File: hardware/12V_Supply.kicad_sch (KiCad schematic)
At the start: 27 parts, among them J1 353180620, J4002 353180620, J4003 353180620, U17 ACS758xCB-150B-PSS

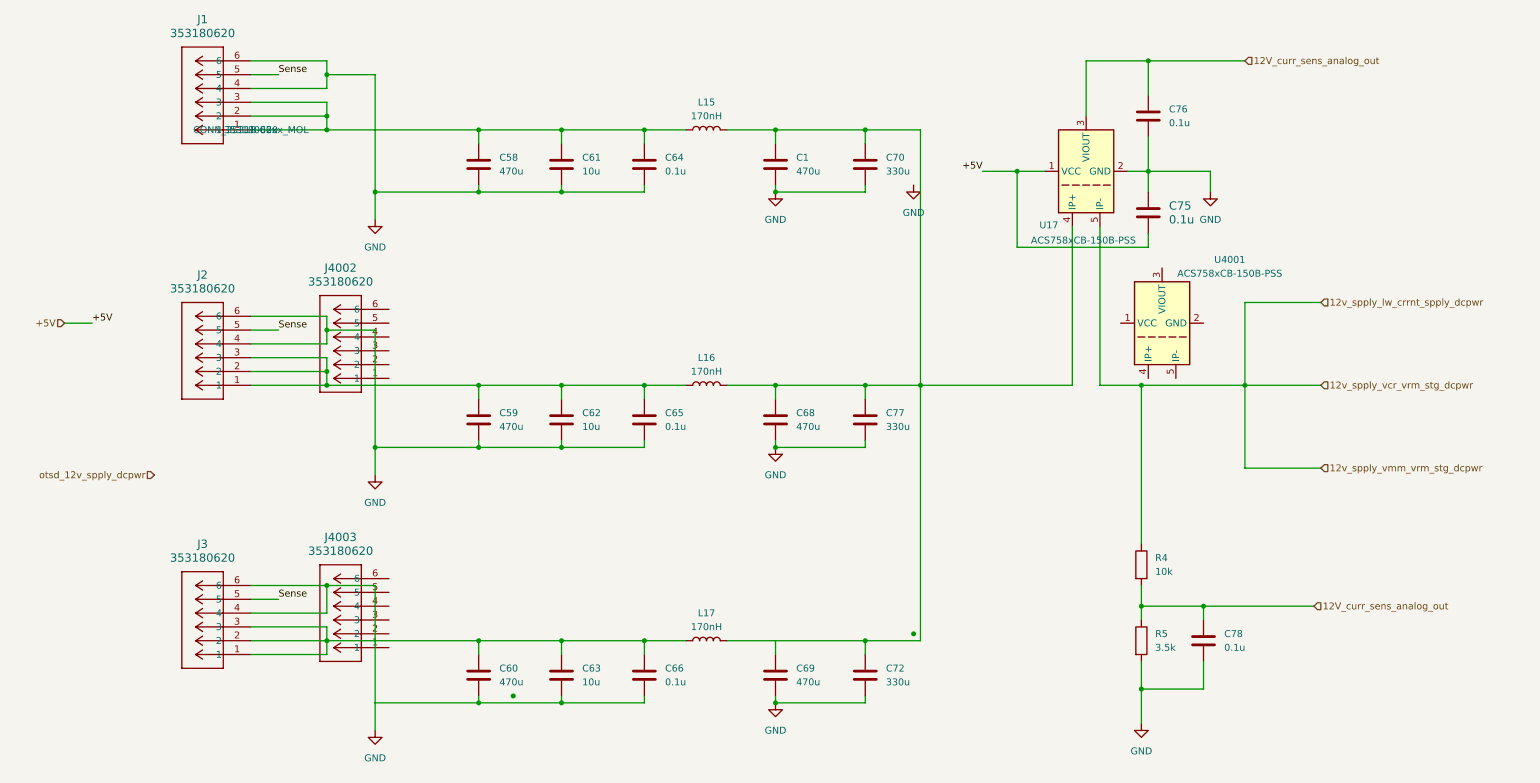
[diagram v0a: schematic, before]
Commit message: fix(schematic): 12V Supply & Low Current Supply
Added proper switching 5V and linear 3.3V ICs.
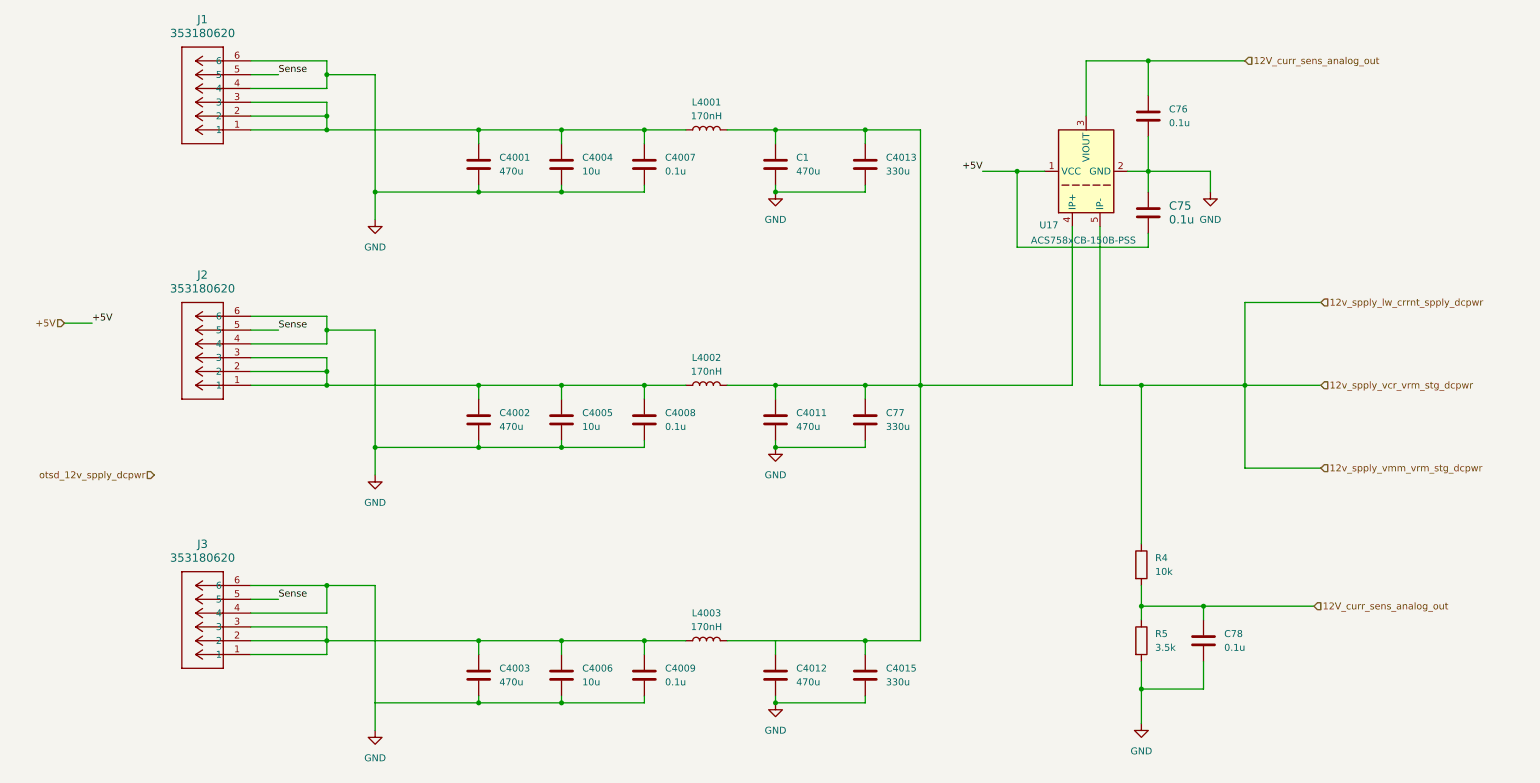
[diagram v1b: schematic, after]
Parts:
- removed J4002, J4003: 353180620, CONN_35318-06xx_MOL, symbol PCIe 2x3 Conn GPU:353180620
- added J2, J3: 353180620, CONN_35318-06xx_MOL, symbol PCIe 2x3 Conn GPU:353180620
- C1, C75, C76, C77, C78: footprint (none) -> Capacitor_SMD:C_0805_2012Metric
- C4001: renamed from C58; footprint (none) -> Capacitor_SMD:C_0805_2012Metric
- C4002: renamed from C59; footprint (none) -> Capacitor_SMD:C_0805_2012Metric
- C4003: renamed from C60; footprint (none) -> Capacitor_SMD:C_0805_2012Metric
- C4004: renamed from C61; footprint (none) -> Capacitor_SMD:C_0805_2012Metric
- C4005: renamed from C62; footprint (none) -> Capacitor_SMD:C_0805_2012Metric
- C4006: renamed from C63; footprint (none) -> Capacitor_SMD:C_0805_2012Metric
- C4007: renamed from C64; footprint (none) -> Capacitor_SMD:C_0805_2012Metric
- C4008: renamed from C65; footprint (none) -> Capacitor_SMD:C_0805_2012Metric
- C4009: renamed from C66; footprint (none) -> Capacitor_SMD:C_0805_2012Metric
- C4011: renamed from C68; footprint (none) -> Capacitor_SMD:C_0805_2012Metric
- C4012: renamed from C69; footprint (none) -> Capacitor_SMD:C_0805_2012Metric
- C4013: renamed from C70; footprint (none) -> Capacitor_SMD:C_0805_2012Metric
- C4015: renamed from C72; footprint (none) -> Capacitor_SMD:C_0805_2012Metric
- renumbered L15 to L4001, L16 to L4002, L17 to L4003
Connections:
- net GND: now also J2.4, J2.6, J3.4, J3.6
- net Sense: now also J2.5, J3.5
- net at C4003.1, C4006.1, C4009.1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: now also J3.1, J3.2, J3.3
- net at C4002.1, C4005.1, C4008.1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: now also J2.1, J2.2, J2.3

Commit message: feat(schematic): 12V and Low Current
Final changes: Added test points and assigned all footprints.
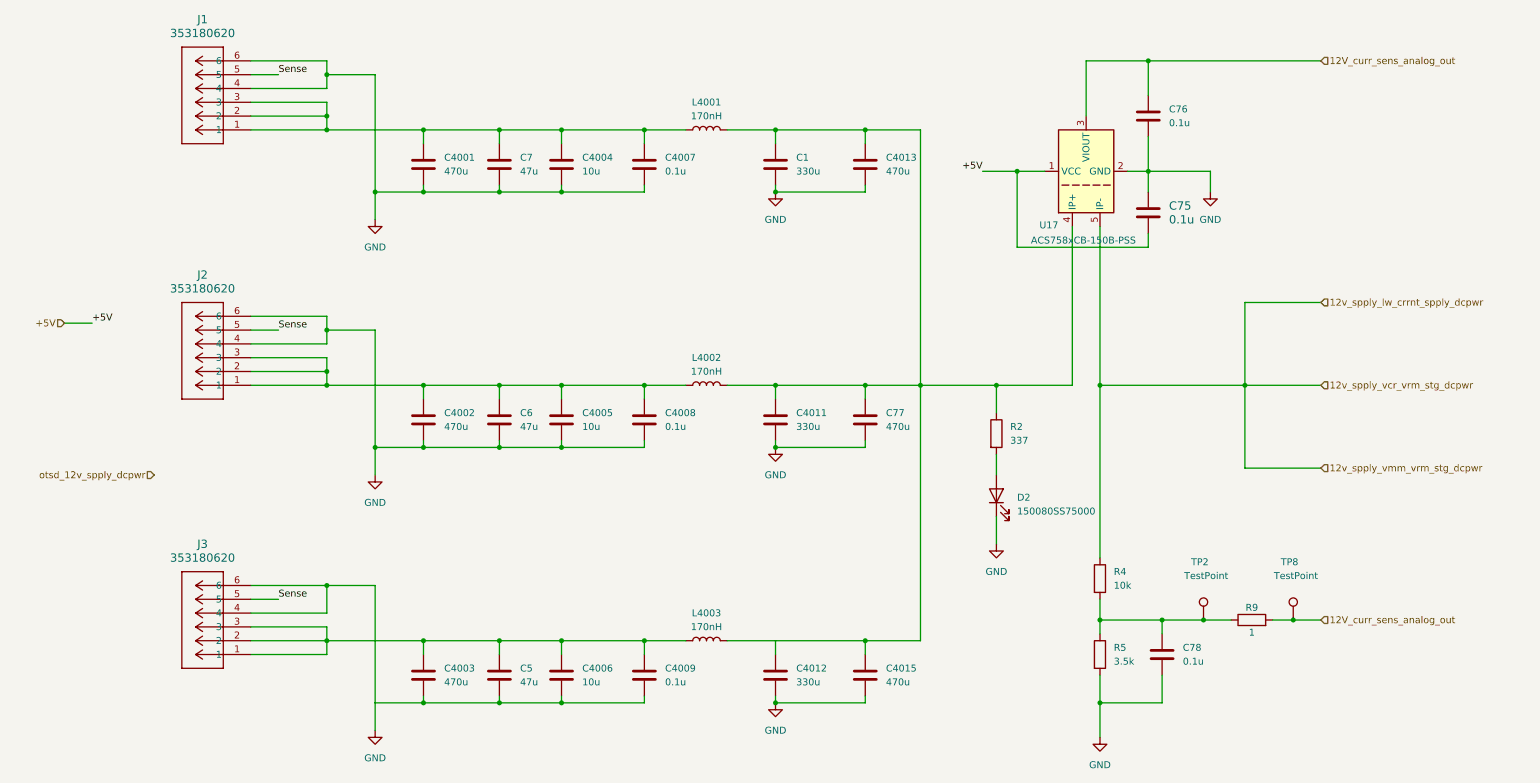
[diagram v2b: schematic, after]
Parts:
- added C5, C6, C7: 47u, Capacitor_SMD:C_0805_2012Metric, symbol Device:C
- added D2: 150080SS75000, LED_SMD:LED_0805_2012Metric_Pad1.15x1.40mm_HandSolder, symbol Device:LED
- added R2: 337, symbol Device:R
- added R9: 1, Resistor_SMD:R_0805_2012Metric, symbol Device:R
- added TP2, TP8: TestPoint, TestPoint:TestPoint_Pad_2.0x2.0mm, symbol Connector:TestPoint
- C1, C4011, C4012: value 470u -> 330u
- C4013, C4015, C77: value 330u -> 470u; footprint Capacitor_SMD:C_0805_2012Metric -> Capacitor_THT:CP_Radial_D8.0mm_P3.50mm
- L4001, L4002: footprint (none) -> 170nH_SMD_Ind:IND_IFLR4031GCERR17M01_VIS-
- L4003: footprint (none) -> 170nH_SMD_Ind:IND_IFLR4031GCERR17M01_VIS-L
- R4, R5: footprint (none) -> Resistor_SMD:R_0805_2012Metric
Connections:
- net 12V_curr_sens_analog_out: now also R9.2, TP8.1; no longer C78.1, R4.2, R5.1
- net GND: now also C5.2, C6.2, C7.2, D2.1 (K)
- net at C1.1, C4011.1, C4012.1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: now also R2.1
- net at C4003.1, C4006.1, C4009.1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: now also C5.1
- net at C4001.1, C4004.1, C4007.1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: now also C7.1
- net at C4002.1, C4005.1, C4008.1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: now also C6.1
- new net: D2.2 (A), R2.2
- new net: C78.1, R4.2, R5.1, R9.1, TP2.1
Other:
- moved on the sheet: C4001, C4002, C4003, C78, R4, R5

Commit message: feat(schematic): 12v supply footprints
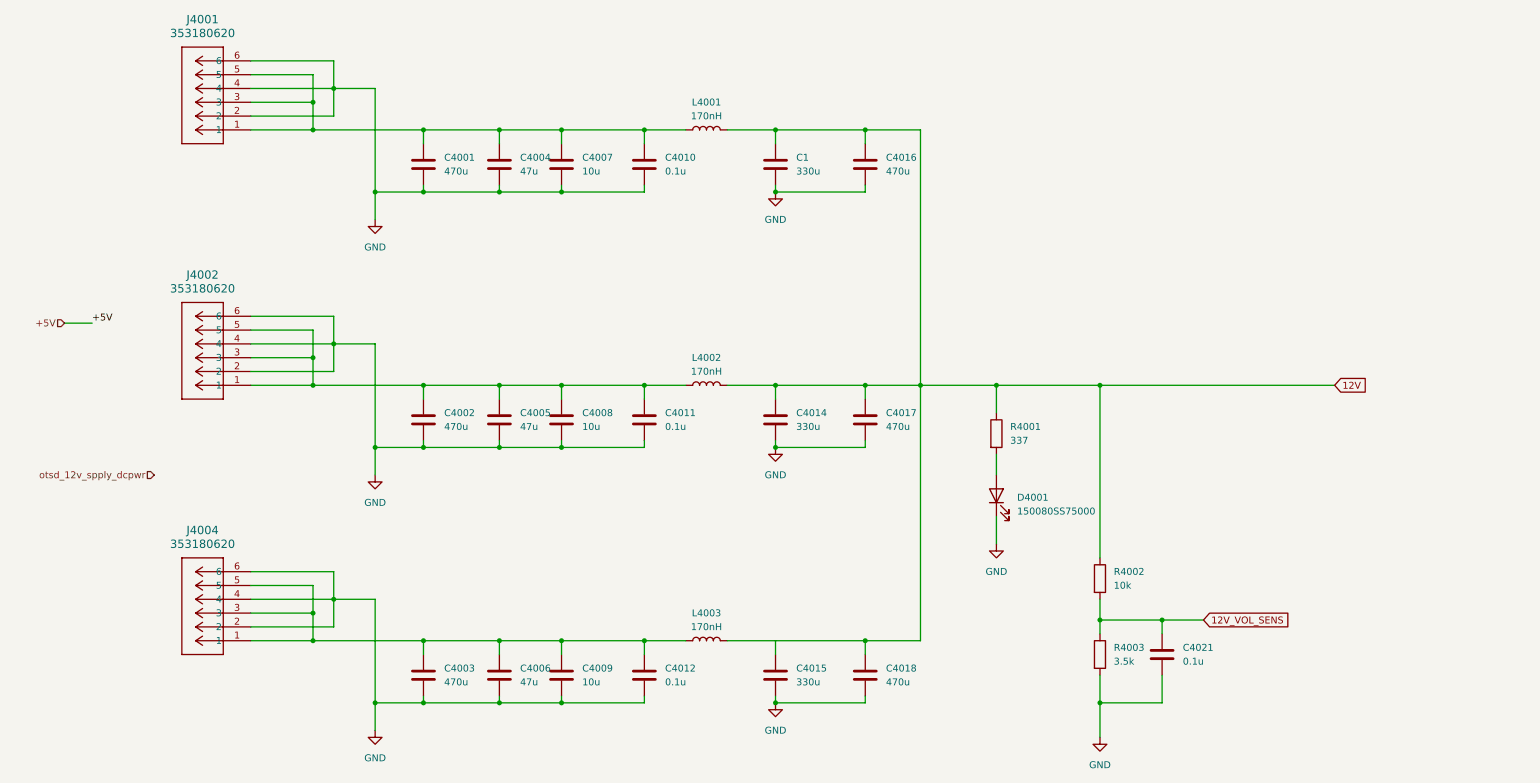
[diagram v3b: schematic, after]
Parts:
- removed C75, C76: 0.1u, Capacitor_SMD:C_0805_2012Metric, symbol Device:C
- removed J1, J3: 353180620, CONN_35318-06xx_MOL, symbol PCIe 2x3 Conn GPU:353180620
- removed R9: 1, Resistor_SMD:R_0805_2012Metric, symbol Device:R
- removed TP2, TP8: TestPoint, TestPoint:TestPoint_Pad_2.0x2.0mm, symbol Connector:TestPoint
- removed U17: ACS758xCB-150B-PSS, Sensor_Current:Allegro_CB_PSS, symbol Sensor_Current:ACS758xCB-150B-PSS
- added J4001, J4004: 353180620, CONN_35318-06xx_MOL, symbol PCIe 2x3 Conn GPU:353180620
- L4001, L4002: footprint 170nH_SMD_Ind:IND_IFLR4031GCERR17M01_VIS- -> 170nH_SMD_Ind:IND_IFLR4031GCERR17M01_VIS-L
- R4001: renamed from R2; footprint (none) -> Resistor_SMD:R_0805_2012Metric
- renumbered C7 to C4004, C6 to C4005, C5 to C4006, C4004 to C4007, C4005 to C4008, C4006 to C4009, C4007 to C4010, C4008 to C4011, C4009 to C4012, C4011 to C4014, C4012 to C4015, C4013 to C4016, C77 to C4017, C4015 to C4018, C78 to C4021, D2 to D4001, J2 to J4002, R4 to R4002, R5 to R4003
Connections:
- net 12v_spply_lw_crrnt_spply_dcpwr is gone; now on net 12V: R4002.1
- net Sense is gone; now on an unnamed net: J4002.5
- net GND: now also J4002.2, J4001.2, J4001.4, J4001.6, J4004.2, J4004.4, J4004.6
- net 12V: now reaches C1.1, C4014.1, C4015.1, C4016.1, C4017.1, C4018.1, L4001.2, L4002.2, L4003.2, R4001.1
- net at C4003.1, C4006.1, C4009.1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: now also J4004.1, J4004.3, J4004.5
- net at C4002.1, C4005.1, C4008.1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: no longer J4002.2
- net at C4001.1, C4004.1, C4007.1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: now also J4001.1, J4001.3, J4001.5
- net 12V_VOL_SENS: now reaches C4021.1, R4002.2, R4003.1

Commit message: feat(PCB): Vrms for mem and core layed out
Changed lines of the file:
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@@
-	(wire
-		(pts
-			(xy 20.32 82.55) (xy 25.4 82.55)
-		)
-		(stroke
-			(width 0)
-			(type default)
-		)
-	)
 	(wire
 		(pts
@@
 			(width 0)
 			(type default)
-		)
-	)
-	(label "+5V"
-		(at 25.4 82.55 0)
-		(fields_autoplaced yes)
-		(effects
-			(font
-				(size 1.27 1.27)
-			)
-			(justify left bottom)
 		)
 	)
@@
 		(fields_autoplaced yes)
 		(effects
-			(font
-				(size 1.27 1.27)
-			)
-			(justify right)
-		)
-	)
-	(hierarchical_label "+5V"
-		(shape input)
-		(at 20.32 82.55 180)
-		(fields_autoplaced yes)
-		(effects

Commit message: feat(PCB): fix all DRC errors
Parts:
- J4001, J4002, J4004: footprint CONN_35318-06xx_MOL -> work:CONN_55690007-SD_06_MOL
- L4001, L4002, L4003: footprint 170nH_SMD_Ind:IND_IFLR4031GCERR17M01_VIS-L -> work:IND_IFLR4031GCERR17M01_VIS
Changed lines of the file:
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@@
 			)
 		)
-		(property "Footprint" "170nH_SMD_Ind:IND_IFLR4031GCERR17M01_VIS-L"
+		(property "Footprint" "work:IND_IFLR4031GCERR17M01_VIS"
 			(at 138.43 140.97 0)
 			(effects
@@
 			)
 		)
-		(property "Footprint" "CONN_35318-06xx_MOL"
+		(property "Footprint" "work:CONN_55690007-SD_06_MOL"
 			(at 54.61 140.97 0)
 			(effects
@@
 			)
 		)
-		(property "Footprint" "170nH_SMD_Ind:IND_IFLR4031GCERR17M01_VIS-L"
+		(property "Footprint" "work:IND_IFLR4031GCERR17M01_VIS"
 			(at 138.43 46.99 0)
 			(effects
@@
 			)
 		)
-		(property "Footprint" "CONN_35318-06xx_MOL"
+		(property "Footprint" "work:CONN_55690007-SD_06_MOL"
 			(at 54.61 46.99 0)
 			(effects
@@
 			)
 		)
-		(property "Footprint" "170nH_SMD_Ind:IND_IFLR4031GCERR17M01_VIS-L"
+		(property "Footprint" "work:IND_IFLR4031GCERR17M01_VIS"
 			(at 138.43 93.98 0)
 			(effects
@@
 			)
 		)
-		(property "Footprint" "CONN_35318-06xx_MOL"
+		(property "Footprint" "work:CONN_55690007-SD_06_MOL"
 			(at 54.61 93.98 0)
 			(effects

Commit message: chore: remove computer control and clean global references
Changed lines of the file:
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@@
-		)
-	)
-	(hierarchical_label "otsd_12v_spply_dcpwr"
-		(shape input)
-		(at 36.83 110.49 180)
-		(fields_autoplaced yes)
-		(effects
-			(font
-				(size 1.27 1.27)
-			)
-			(justify right)
 		)
 	)

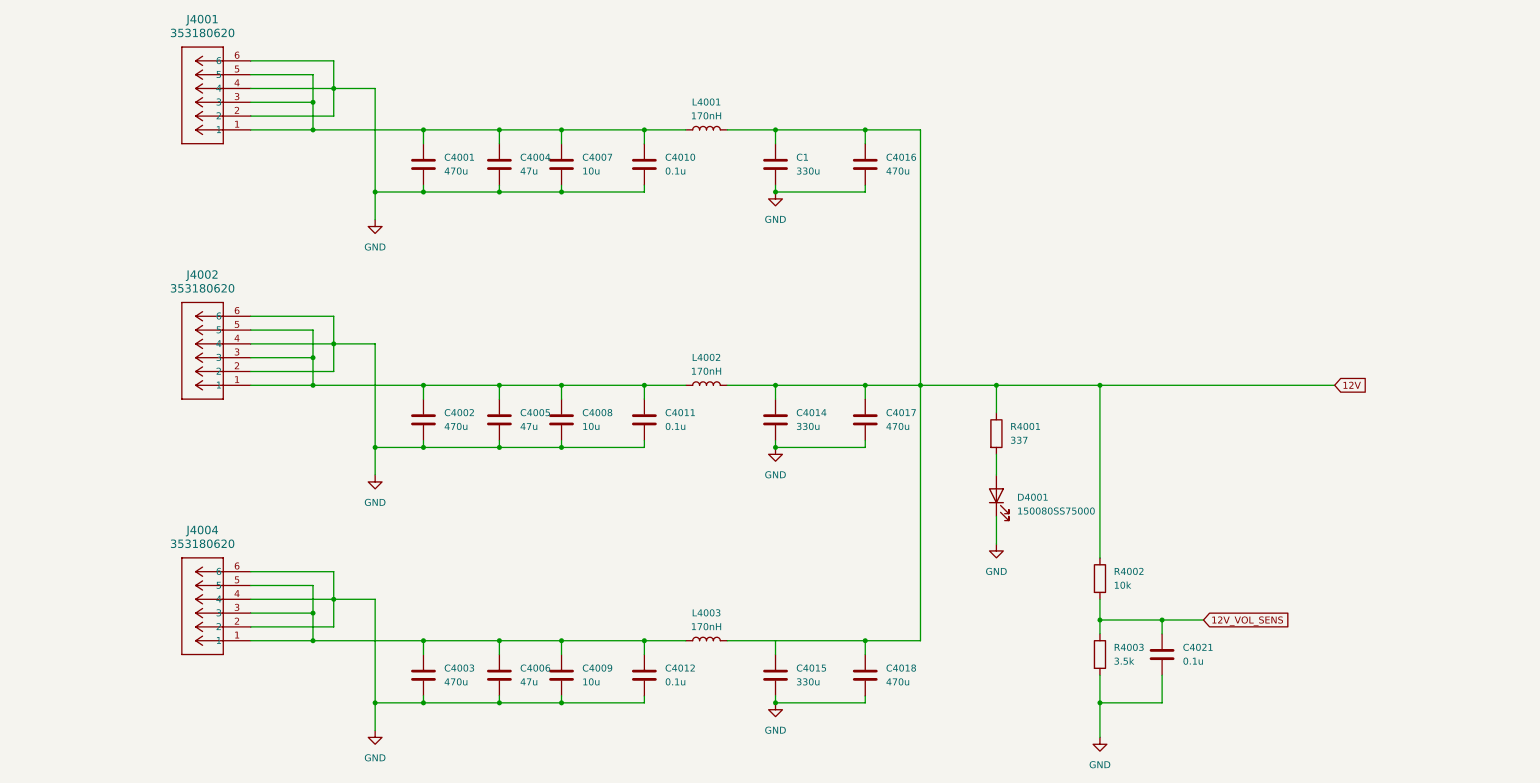
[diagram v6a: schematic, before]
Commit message: feat(schematic): refactor main heirarchy
This commit makes a bunch of changes to how power is delivered on the
schematic. It also adds the probit header and the i2c output connector
on the main page of the schematic. Lastly, it changes it so that USB
power should work and also not power the 5V rail to the mosfet ICs.
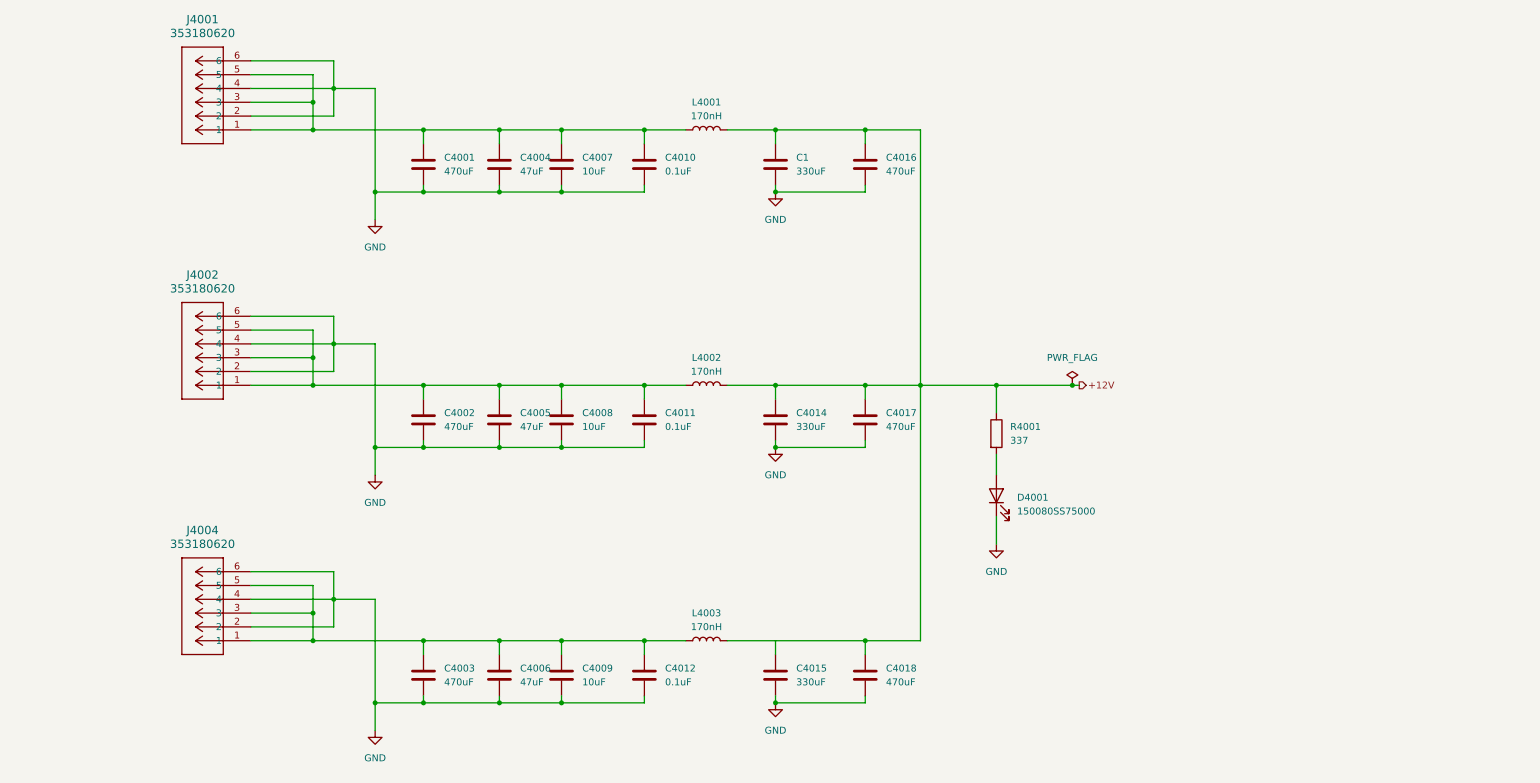
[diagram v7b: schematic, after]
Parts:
- removed C4021: 0.1u, Capacitor_SMD:C_0805_2012Metric, symbol Device:C
- removed R4002: 10k, Resistor_SMD:R_0805_2012Metric, symbol Device:R
- removed R4003: 3.5k, Resistor_SMD:R_0805_2012Metric, symbol Device:R
- C1, C4014, C4015: value 330u -> 330uF
- C4001, C4002, C4003, C4016, C4017, C4018: value 470u -> 470uF
- C4004, C4005, C4006: value 47u -> 47uF
- C4007, C4008, C4009: value 10u -> 10uF
- C4010, C4011, C4012: value 0.1u -> 0.1uF
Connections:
- net 12V renamed +12V
